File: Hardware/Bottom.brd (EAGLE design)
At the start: 120 x 80 mm, 105 parts, among them IC1 OP491SOIC_N14, IC3 74LVC1G17DCK, IC4 LT6231, IC5 SN74CBT3253SOIC16, Q2 25MHz

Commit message: m
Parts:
- C1, C2, C3, C4, C40, C41, C47, C48, C49, C50: device rcl:C0402 -> rcl:C0603
- C15, C16, C8, C9: value 10µ -> 4µ7
- C24: device rcl:C0402 -> rcl:C0805
- C28: value 1µ -> 4µ7; device rcl:C0603 -> rcl:C0805
- C29, C30: value 2µ -> 4µ7
- L3, L4: device rcl:L3216C -> rcl:L2012C
- R12, R13: device rcl:M0805 -> rcl:R0603
- R5, R6: device rcl:R0402 -> rcl:R0603
- moved R6 3.20 mm to (17.0, 42.9), turned to 90 degrees
- moved R5 1.46 mm to (15.2, 60.0), turned to 0 degrees
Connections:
- removed net N$49: C15.1
- net VDD_DC: now also C15.1
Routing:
- net VDD_DC: track 11.5 -> 3.40 mm
- net VREG_VDD5_EN: track 1.84 -> 5.42 mm
- net VREG_VDD3V3_EN: track 1.84 -> 2.92 mm
- net +3V3: track 47.4 -> 48.1 mm

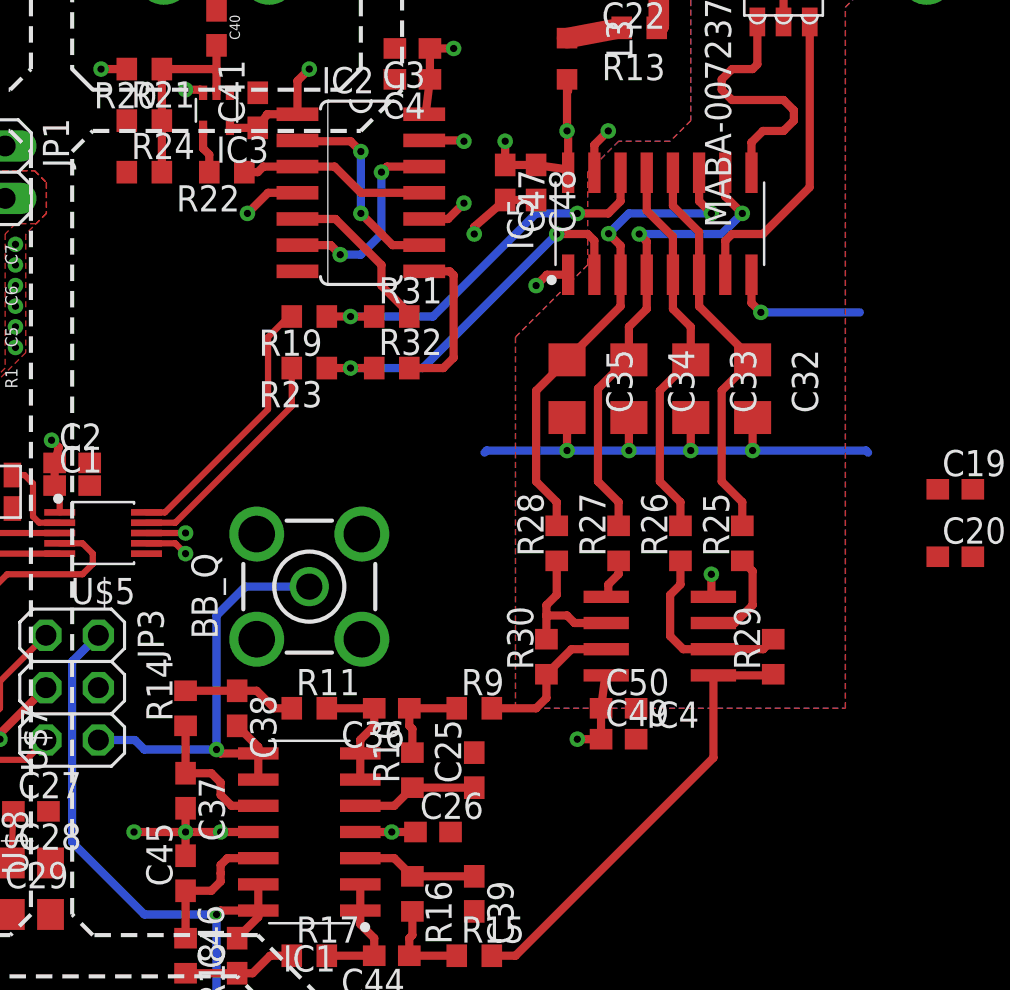
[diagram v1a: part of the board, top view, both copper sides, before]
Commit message: Add KiCAD Bottom
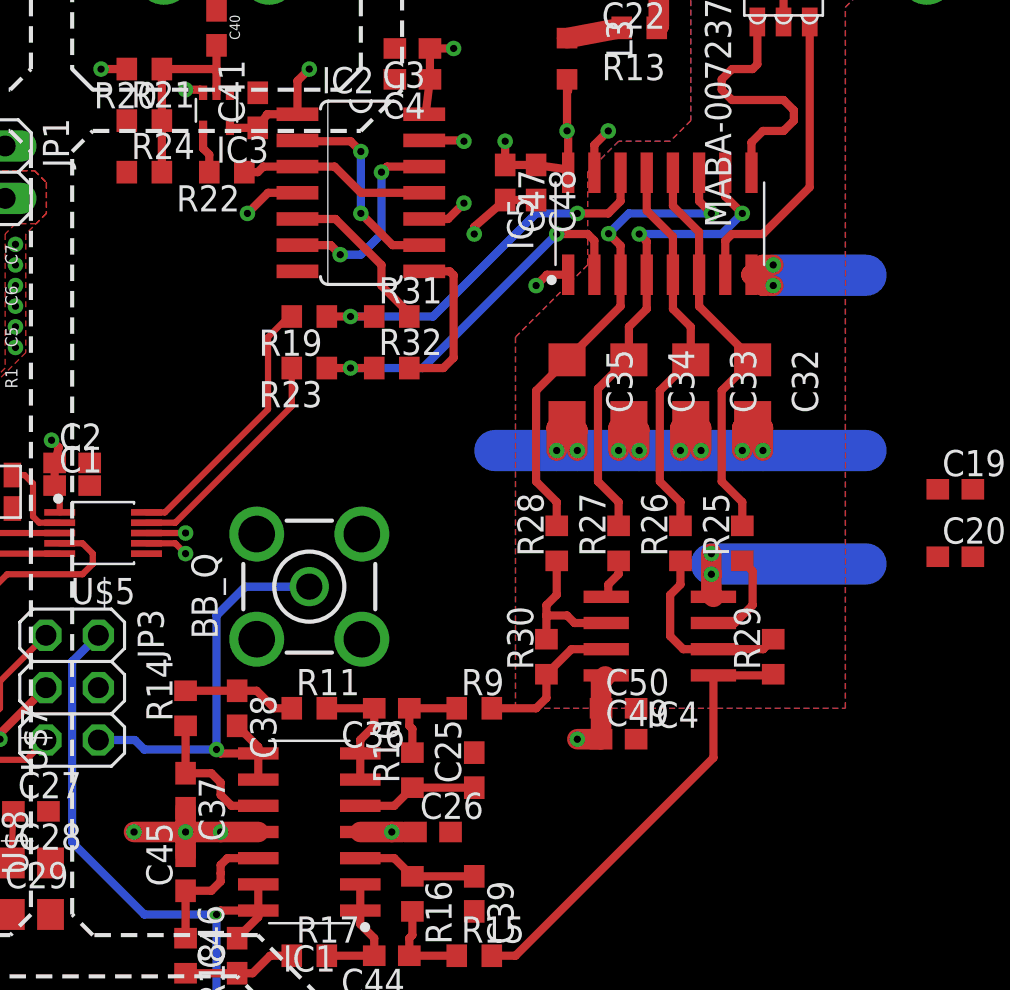
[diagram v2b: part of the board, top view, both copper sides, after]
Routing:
- net GND: track 69.7 -> 78.3 mm, vias 37 -> 43
- net N$9: track 0.00 -> 7.50 mm

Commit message: Update board Projektarbeit
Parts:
- removed C10, C11, C19, C20: 100n, rcl:C0603
- removed C6, C7: 22µ, rcl:C0805
- removed C8, C9: 4µ7, rcl:C0805
- removed L1: 4.7µH, PowerMagnetics (rev18d):WE-MAPI_3015/3020
- removed R1: 54k9, rcl:R0603
- removed R2, R6: 10k, rcl:R0603
- removed SV3: (no value), con-lstb:MA05-2
- removed U$2: TPS562201, MyLib:SOT95P280X110-6
- added C43: 22µ, rcl:C0805
- added D1: (no value), diode:SMB
- added TST1, TST2, TST3, TST4: BU-SMA-V, con-coax:BU-SMA-V
- C17, C18: device rcl:C0603 -> rcl:C0805
- C5: value 22µ -> 4µ7
- R3, R4, R5: device rcl:R0603 -> rcl:R0805
- moved RF_IN 37.0 mm to (37.0, 61.5)
- moved C40 36.8 mm to (10.5, 38.5)
- moved LO_IN 36.8 mm to (10.5, 43.5), turned to 90 degrees
- moved R20 36.0 mm to (10.5, 34.5), turned to 270 degrees
- moved C3 34.2 mm to (15.0, 48.5)
- moved C4 34.0 mm to (16.0, 45.5), turned to 270 degrees
- moved JP1 32.9 mm to (13.5, 27.5), turned to 0 degrees
- moved R21 32.8 mm to (12.5, 34.5), turned to 90 degrees
- moved IC3 32.5 mm to (13.5, 37.5), turned to 270 degrees
- moved R24 29.6 mm to (14.5, 34.5), turned to 90 degrees
- moved C41 29.4 mm to (16.0, 41.5)
- moved R12 28.9 mm to (31.0, 59.0)
- moved R22 27.2 mm to (18.0, 38.0)
- moved R13 26.9 mm to (31.0, 56.5)
- moved C21 26.4 mm to (42.5, 61.5), turned to 0 degrees
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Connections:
- removed net +5V: JP1.1, SV3.2, SV3.4
- removed net N$11: R1.2, R2.2, U$2.4
- removed net N$30: C5.1, C6.1, C7.1, JP1.2, L1.2, R1.1
- removed net N$35: SV4.10
- removed net N$36: SV4.8
- removed net N$37: SV4.6
- removed net N$38: SV4.4
- removed net N$8: C11.2, L1.1, U$2.2
- removed net RESV_NC: SV4.2
- removed net SPI_MCS_MOSI: SV4.7
- removed net VREG_VDD5_EN: R6.1, U$2.5
- new net FBPEIHRNG: TST3.1
- new net TST1: TST1.1
- new net TST2: TST2.1
- new net TST4: TST4.1
- new net VCCADC: C30.1, C31.1, JP1.1, L4.1, U$7.16
- net +3V3: now also JP1.2, SV4.10, SV4.8; no longer C19.1, C20.1, C30.1, C31.1, SV3.6, SV3.8, U$7.16
- net ADC_CHSEL: now also SV4.3; no longer SV4.1
- net BASEBAND_I: now also JP3.6; no longer JP3.2
- net BASEBAND_Q: now also JP3.2; no longer JP3.6
- net GND: now also C43.2, SV4.1, SV4.2, TST1.2, TST1.3, TST1.4, TST1.5, TST2.2, TST2.3, TST2.4, TST2.5, TST3.2, TST3.3, TST3.4, TST3.5, TST4.2, TST4.3, TST4.4, TST4.5; no longer C10.2, C19.2, C20.2, C6.2, C7.2, C8.2, C9.2, R2.1, SV3.1, SV3.3, SV3.5, SV3.7, U$2.1
- net I2C_MCS_SCL: now also SV4.4; no longer SV3.9
- net I2C_MCS_SDA: now also SV4.6; no longer SV3.10
- net N$31: now also C43.1
- net N$56: now also Q2.3; no longer Q2.4
- net N$7: now also D1.A, J1.3; no longer C11.1, U$2.6
- net SPI_MCS_CLK: now also SV4.7; no longer SV4.9
- net SPI_MCS_CS: now also SV4.5; no longer SV4.3
- net SPI_MCS_MISO: now also SV4.9; no longer SV4.5
- net VDD_DC: now also C5.1, D1.C; no longer C10.1, C8.1, C9.1, J1.3, R6.2, U$2.3
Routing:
- net GND: track 78.3 -> 119.5 mm, vias 43 -> 73
- net +3V3: track 48.2 -> 74.1 mm, vias 13 -> 60
- net N$57: track 21.6 -> 6.93 mm
- net N$11: track 12.9 -> 0.00 mm, vias 2 -> 1
- net N$1: track 13.0 -> 2.05 mm
- net VCCADC: track 0.00 -> 10.4 mm
- net TST4: track 0.00 -> 10.2 mm, vias 0 -> 3
- net TST2: track 0.00 -> 10.2 mm, vias 0 -> 3
- net TST1: track 0.00 -> 10.2 mm, vias 0 -> 3
- net FBPEIHRNG: track 0.00 -> 10.1 mm, vias 0 -> 3
- net ADC_CHSEL: track 22.7 -> 13.4 mm
- net N$51: track 13.0 -> 3.65 mm
- net CLK_Q: track 18.6 -> 27.0 mm
- net N$9: track 7.50 -> 0.00 mm, vias 0 -> 1
- net N$32: track 3.79 -> 10.8 mm
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- added copper zone on layer 1, net NOFILL
- added copper zone on layer 15, net NOFILL
- added copper zone on layer 16, net NOFILL
- added copper zone on layer 2, net NOFILL
- removed copper zone on layer 1, net CUTOUT
- removed copper zone on layer 15, net CUTOUT
- removed copper zone on layer 16, net CUTOUT
- removed copper zone on layer 2, net CUTOUT
- removed copper zone on layer 1, net N$19
- removed copper zone on layer 2, net N$19
- removed copper zone on layer 1, net N$30
- removed copper zone on layer 1, net N$8
- removed copper zone on layer 2, net N$8
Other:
- outline, holes or cut-outs redrawn
- board text added: "+3V3"
- board text added: "GND"

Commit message: KiCAD advancements
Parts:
- moved C22 16.0 mm to (47.0, 65.0), turned to 0 degrees
- moved C48 14.2 mm to (42.0, 40.0), turned to 0 degrees
- moved C47 12.5 mm to (37.0, 40.0)
- moved C35 12.2 mm to (46.5, 43.0)
- moved L3 11.2 mm to (33.0, 65.0)
- moved C23 10.8 mm to (47.0, 59.0), turned to 0 degrees
- moved C34 10.3 mm to (32.5, 50.0), turned to 90 degrees
- moved C24 10.3 mm to (47.0, 62.0), turned to 0 degrees
- moved C32 9.49 mm to (46.5, 50.0), turned to 90 degrees
- moved C33 8.25 mm to (32.5, 43.0)
- moved RF_IN 6.26 mm to (40.0, 67.0)
- moved R13 5.85 mm to (33.0, 62.0)
- moved U$6 4.47 mm to (40.0, 58.0)
- moved C21 2.55 mm to (40.0, 62.0)
- moved R12 2.24 mm to (33.0, 58.0)
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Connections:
- removed net N$23: C34.1, IC5.10, IC5.4, R27.2
- removed net N$53: C33.1, IC5.13, IC5.5, R26.2
- new net N$128: C35.1, IC5.11, IC5.3, R26.2
- new net N$130: C33.1, IC5.13, IC5.5, R27.2
- net N$34: now also C34.1, IC5.10, IC5.4; no longer C35.1, IC5.11, IC5.3
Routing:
- net GND: track 119.5 -> 91.6 mm, vias 73 -> 72
- net N$23: track 22.0 -> 0.00 mm, vias 2 -> 0
- net N$53: track 17.5 -> 0.00 mm
- net N$18: track 16.3 -> 0.00 mm
- net N$34: track 22.6 -> 9.95 mm
- net N$24: track 18.3 -> 7.65 mm
- net N$128: track 0.00 -> 9.84 mm, vias 0 -> 2
- net CLK_I: track 24.8 -> 15.0 mm
- net +3V3: track 74.1 -> 66.3 mm, vias 60 -> 58
- net N$52: track 10.4 -> 3.61 mm
- net CLK_Q: track 27.0 -> 20.9 mm
- net N$130: track 0.00 -> 5.47 mm
- net N$17: track 5.17 -> 0.00 mm
- net N$16: track 4.65 -> 0.00 mm
- net N$51: track 3.65 -> 0.08 mm
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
